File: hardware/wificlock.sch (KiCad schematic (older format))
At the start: 41 parts, among them J1 USB_C_Receptacle_USB2.0, Q1 AO3402, Q2 AO3402, Q3 AO3402, Q4 AO3402, SW1 SW_SPST, SW2 SW_SPST, SW3 SW_SPST, U1 CH340G, U2 ESP-12F, U3 ME6211C33M5G, Y1 12MHz

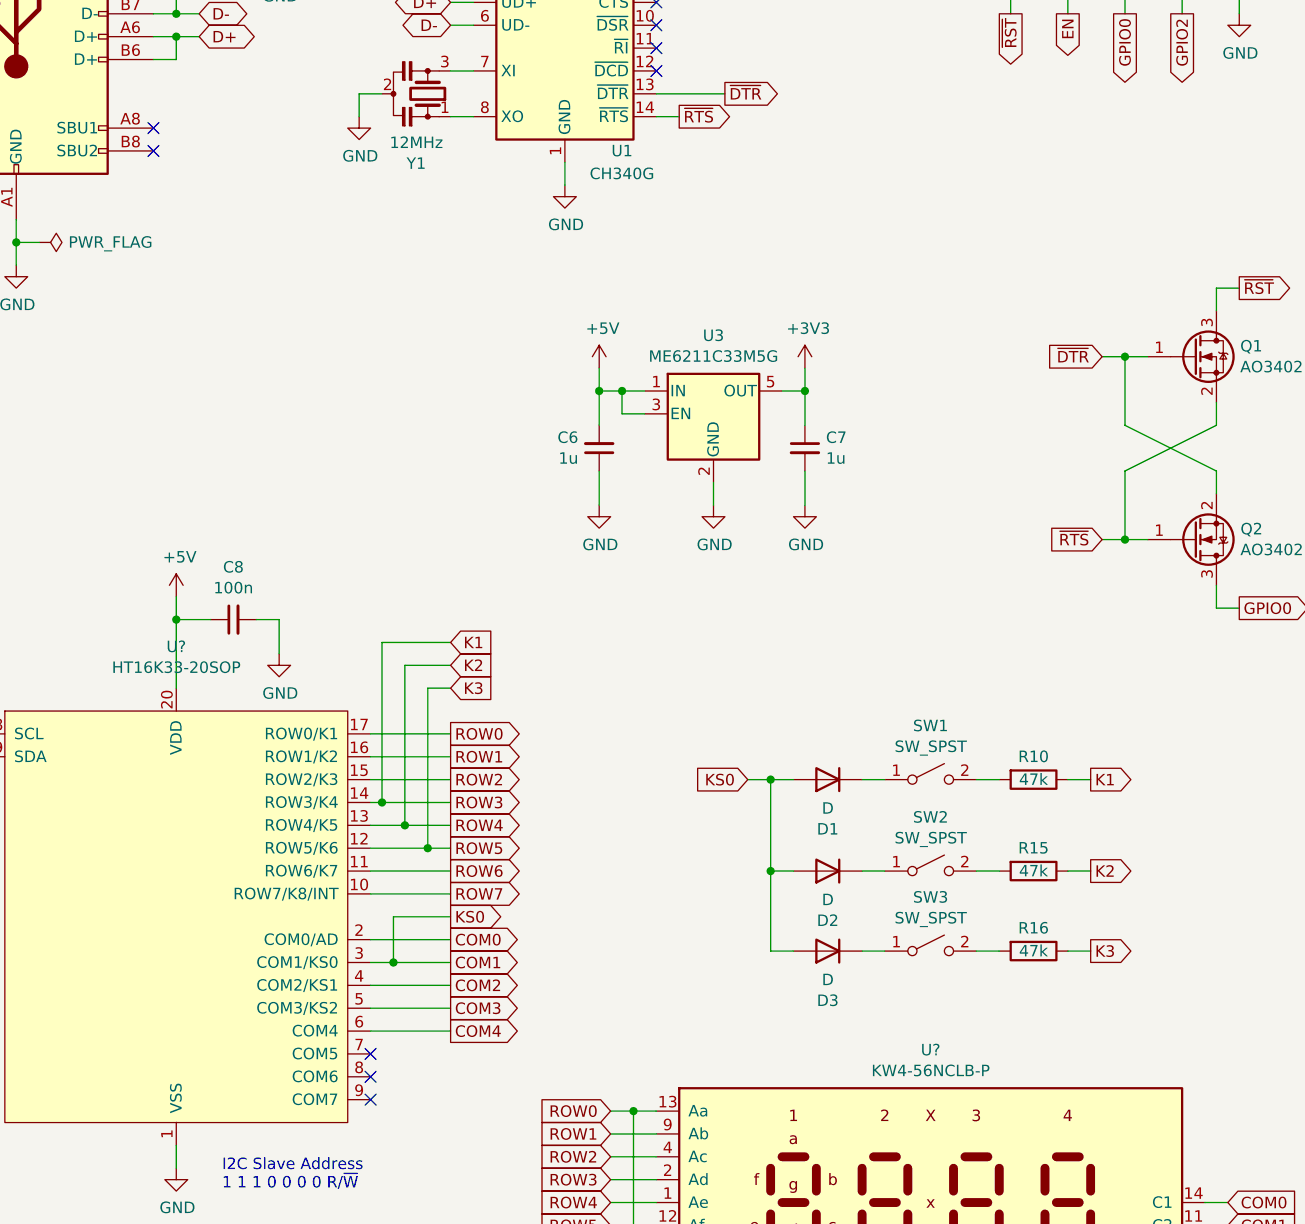
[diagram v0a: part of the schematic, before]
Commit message: add footprints for display and tactile side switch
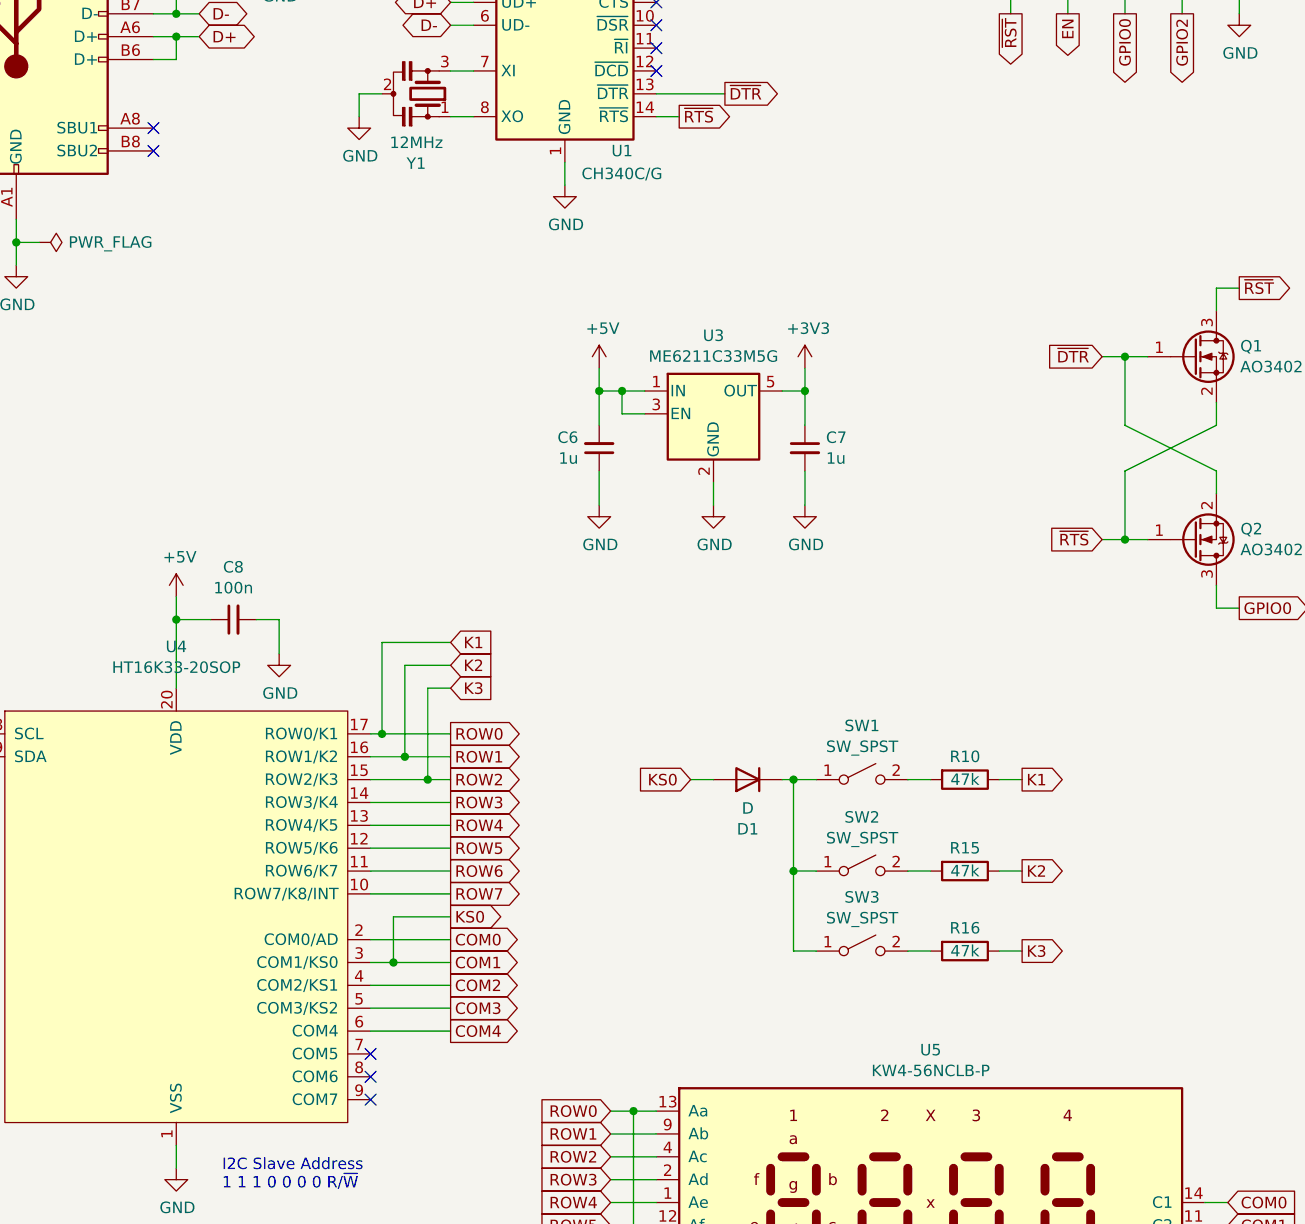
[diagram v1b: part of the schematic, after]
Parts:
- removed D2, D3: D, symbol Device:D
- D1: footprint (none) -> Diode_SMD:D_SOD-123
- R11, R12, R13, R14: footprint (none) -> Resistor_SMD:R_0805_2012Metric
- SW1, SW2, SW3: footprint (none) -> wificlock:Switch-Tactile-3x6x3.5
- U1: value CH340G -> CH340C/G
- U5: renamed from U?; footprint (none) -> wificlock:KW4-56NXLB-P
- Y1: footprint (none) -> Crystal:Resonator_SMD_muRata_CSTxExxV-3Pin_3.0x1.1mm
- gave numbers to parts that had none: 1
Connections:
- net ROW0 is gone; now on net K1: U4.17 (ROW0/K1), U5.13 (Aa), U5.8 (Ax)
- net ROW1 is gone; now on net K2: U4.16 (ROW1/K2), U5.9 (Ab)
- net ROW2 is gone; now on net K3: U4.15 (ROW2/K3), U5.4 (Ac)
- net K1: no longer U4.14 (ROW3/K4), U5.2 (Ad)
- net K2: no longer U4.13 (ROW4/K5), U5.1 (Ae)
- net K3: no longer U4.12 (ROW5/K6), U5.12 (Af)
- net at D1.1 (K), SW1.1 (A): now also SW2.1 (A), SW3.1 (A)
- new net ROW3: U4.14 (ROW3/K4), U5.2 (Ad)
- new net ROW4: U4.13 (ROW4/K5), U5.1 (Ae)
- new net ROW5: U4.12 (ROW5/K6), U5.12 (Af)
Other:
- moved on the sheet: D1, R10, R15, R16, SW1, SW2, SW3
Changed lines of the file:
@@
 P 3550 1700
 F 0 "U1" H 3800 1150 50  0000 C CNN
-F 1 "CH340G" H 3800 1050 50  0000 C CNN
+F 1 "CH340C/G" H 3800 1050 50  0000 C CNN
 F 2 "Package_SO:SOIC-16_3.9x9.9mm_P1.27mm" H 3600 1150 50  0001 L CNN
 F 3 "https://www.mpja.com/download/35227cpdata.pdf" H 3200 2500 50  0001 C CNN
@@
 F 0 "Y1" V 2645 1950 50  0000 C CNN
 F 1 "12MHz" V 2736 1950 50  0000 C CNN
-F 2 "" H 2925 2000 50  0001 C CNN
+F 2 "Crystal:Resonator_SMD_muRata_CSTxExxV-3Pin_3.0x1.1mm" H 2925 2000 50  0001 C CNN
 F 3 "~" H 2925 2000 50  0001 C CNN
 	1    2950 2000
@@
 Wire Wire Line
 	2800 5800 3050 5800
-Text GLabel 4350 5000 0    50   Input ~ 0
-KS0
-$Comp
-L Device:D D1
-U 1 1 60484D0D
-P 4700 5000
-F 0 "D1" H 4700 5217 50  0000 C CNN
-F 1 "D" H 4700 5126 50  0000 C CNN
-F 2 "" H 4700 5000 50  0001 C CNN
-F 3 "~" H 4700 5000 50  0001 C CNN
-	1    4700 5000
-	-1   0    0    1
-$EndComp
-$Comp
-L Switch:SW_SPST SW1
-U 1 1 60486161
-P 5150 5000
-F 0 "SW1" H 5150 5235 50  0000 C CNN
-F 1 "SW_SPST" H 5150 5144 50  0000 C CNN
-F 2 "" H 5150 5000 50  0001 C CNN
-F 3 "~" H 5150 5000 50  0001 C CNN
-	1    5150 5000
-	1    0    0    -1
-$EndComp
-Wire Wire Line
-	4950 5000 4850 5000
-Wire Wire Line
-	4450 5000 4350 5000
-Wire Wire Line
-	4550 5000 4450 5000
-$Comp
-L Device:D D2
-U 1 1 60566D9D
-P 4700 5400
-F 0 "D2" H 4700 5617 50  0000 C CNN
-F 1 "D" H 4700 5526 50  0000 C CNN
-F 2 "" H 4700 5400 50  0001 C CNN
-F 3 "~" H 4700 5400 50  0001 C CNN
-	1    4700 5400
-	-1   0    0    1
-$EndComp
-$Comp
-L Switch:SW_SPST SW2
-U 1 1 605672B7
-P 5150 5400
-F 0 "SW2" H 5150 5635 50  0000 C CNN
-F 1 "SW_SPST" H 5150 5544 50  0000 C CNN
-F 2 "" H 5150 5400 50  0001 C CNN
-F 3 "~" H 5150 5400 50  0001 C CNN
-	1    5150 5400
-	1    0    0    -1
-$EndComp
-Text GLabel 5850 5400 2    50   Output ~ 0
-K2
-Wire Wire Line
-	5850 5400 5750 5400
-Wire Wire Line
-	4950 5400 4850 5400
-Wire Wire Line
-	4450 5000 4450 5400
-Wire Wire Line
-	4450 5400 4550 5400
-Connection ~ 4450 5000
-$Comp
-L Device:D D3
-U 1 1 60586F2B
-P 4700 5750
-F 0 "D3" H 4700 5967 50  0000 C CNN
-F 1 "D" H 4700 5876 50  0000 C CNN
-F 2 "" H 4700 5750 50  0001 C CNN
-F 3 "~" H 4700 5750 50  0001 C CNN
-	1    4700 5750
-	-1   0    0    1
-$EndComp
-Wire Wire Line
-	4450 5400 4450 5750
-Wire Wire Line
-	4450 5750 4550 5750
-Connection ~ 4450 5400
-$Comp
-L Switch:SW_SPST SW3
-U 1 1 60592409
-P 5150 5750
-F 0 "SW3" H 5150 5985 50  0000 C CNN
-F 1 "SW_SPST" H 5150 5894 50  0000 C CNN
-F 2 "" H 5150 5750 50  0001 C CNN
-F 3 "~" H 5150 5750 50  0001 C CNN
-	1    5150 5750
-	1    0    0    -1
-$EndComp
-Text GLabel 5850 5750 2    50   Output ~ 0
-K3
-Wire Wire Line
-	5850 5750 5750 5750
-Wire Wire Line
-	4950 5750 4850 5750
 $Comp
 L power:GND #PWR027
@@
 Wire Wire Line
 	2300 4300 2300 4450
-$Comp
-L Device:R R10
-U 1 1 6067C984
-P 5600 5000
-F 0 "R10" V 5500 5000 50  0000 C CNN
-F 1 "47k" V 5600 5000 50  0000 C CNN
-F 2 "Resistor_SMD:R_0805_2012Metric" V 5530 5000 50  0001 C CNN
-F 3 "~" H 5600 5000 50  0001 C CNN
-	1    5600 5000
-	0    1    1    0
-$EndComp
 Text GLabel 3050 5100 2    50   Output ~ 0
 ROW3
-Wire Wire Line
-	2700 5000 3050 5000
 Text GLabel 3050 5000 2    50   Output ~ 0
 ROW2
-Wire Wire Line
-	2700 4900 3050 4900
 Text GLabel 3050 4900 2    50   Output ~ 0
 ROW1
-Wire Wire Line
-	2700 4800 3050 4800
 Text GLabel 3050 4800 2    50   Output ~ 0
 ROW0
@@
 Wire Wire Line
 	3050 4400 2750 4400
-Wire Wire Line
-	2750 5100 3050 5100
-Wire Wire Line
-	2700 5100 2750 5100
-Connection ~ 2750 5100
-Wire Wire Line
-	2750 4400 2750 5100
-Wire Wire Line
-	2950 5300 2700 5300
-Wire Wire Line
-	2950 4600 2950 5300
 Text GLabel 3050 4600 2    50   Input ~ 0
 K3
 Wire Wire Line
 	3050 4600 2950 4600
-Wire Wire Line
-	2850 5200 2700 5200
-Wire Wire Line
-	2850 4500 2850 5200
 Text GLabel 3050 4500 2    50   Input ~ 0
 K2
 Wire Wire Line
 	3050 4500 2850 4500
-Wire Wire Line
-	5850 5000 5750 5000
-Text GLabel 5850 5000 2    50   Output ~ 0
-K1
 Text Notes 2050 6800 0    50   ~ 0
 I2C Slave Address\n1 1 1 0 0 0 0 R/~W~
-Wire Wire Line
-	5450 5000 5350 5000
-$Comp
-L Device:R R15
-U 1 1 607456CB
-P 5600 5400
-F 0 "R15" V 5500 5400 50  0000 C CNN
-F 1 "47k" V 5600 5400 50  0000 C CNN
-F 2 "Resistor_SMD:R_0805_2012Metric" V 5530 5400 50  0001 C CNN
-F 3 "~" H 5600 5400 50  0001 C CNN
-	1    5600 5400
-	0    1    1    0
-$EndComp
-Wire Wire Line
-	5450 5400 5350 5400
-$Comp
-L Device:R R16
-U 1 1 60745A32
-P 5600 5750
-F 0 "R16" V 5500 5750 50  0000 C CNN
-F 1 "47k" V 5600 5750 50  0000 C CNN
-F 2 "Resistor_SMD:R_0805_2012Metric" V 5530 5750 50  0001 C CNN
-F 3 "~" H 5600 5750 50  0001 C CNN
-	1    5600 5750
-	0    1    1    0
-$EndComp
-Wire Wire Line
-	5450 5750 5350 5750
 $Comp
 L Device:R R14
@@
 F 0 "R14" H 9870 5146 50  0000 L CNN
 F 1 "4k7" H 9870 5055 50  0000 L CNN
-F 2 "" V 9730 5100 50  0001 C CNN
+F 2 "Resistor_SMD:R_0805_2012Metric" V 9730 5100 50  0001 C CNN
 F 3 "~" H 9800 5100 50  0001 C CNN
 	1    9800 5100
@@
 F 0 "R12" H 8670 5146 50  0000 L CNN
 F 1 "4k7" H 8670 5055 50  0000 L CNN
-F 2 "" V 8530 5100 50  0001 C CNN
+F 2 "Resistor_SMD:R_0805_2012Metric" V 8530 5100 50  0001 C CNN
 F 3 "~" H 8600 5100 50  0001 C CNN
 	1    8600 5100
@@
 F 0 "R13" H 9570 5146 50  0000 L CNN
 F 1 "4k7" H 9570 5055 50  0000 L CNN
-F 2 "" V 9430 5100 50  0001 C CNN
+F 2 "Resistor_SMD:R_0805_2012Metric" V 9430 5100 50  0001 C CNN
 F 3 "~" H 9500 5100 50  0001 C CNN
 	1    9500 5100
@@
 F 0 "R11" H 8370 5146 50  0000 L CNN
 F 1 "4k7" H 8370 5055 50  0000 L CNN
-F 2 "" V 8230 5100 50  0001 C CNN
+F 2 "Resistor_SMD:R_0805_2012Metric" V 8230 5100 50  0001 C CNN
 F 3 "~" H 8300 5100 50  0001 C CNN
 	1    8300 5100
@@
 Text GLabel 3050 5200 2    50   Output ~ 0
 ROW4
-Wire Wire Line
-	2850 5200 3050 5200
-Connection ~ 2850 5200
 Text GLabel 3050 5300 2    50   Output ~ 0
 ROW5
-Wire Wire Line
-	2950 5300 3050 5300
-Connection ~ 2950 5300
 Text GLabel 3050 5400 2    50   Output ~ 0
 ROW6
@@
 NoConn ~ 2700 6400
 $Comp
-L wificlock:KW4-56NCLB-P U?
+L wificlock:KW4-56NCLB-P U5
 U 1 1 602B0D2E
 P 5150 6850
-F 0 "U?" H 5150 7517 50  0000 C CNN
+F 0 "U5" H 5150 7517 50  0000 C CNN
 F 1 "KW4-56NCLB-P" H 5150 7426 50  0000 C CNN
-F 2 "" H 5500 6550 50  0001 C CNN
+F 2 "wificlock:KW4-56NXLB-P" H 5500 6550 50  0001 C CNN
 F 3 "https://cdn-shop.adafruit.com/datasheets/865datasheet.pdf" H 5500 6550 50  0001 C CNN
 	1    5150 6850
@@
 $EndComp
 $Comp
-L wificlock:HT16K33-20SOP U?
+L wificlock:HT16K33-20SOP U4
 U 1 1 602D3B7B
 P 1850 5600
-F 0 "U?" H 1850 6781 50  0000 C CNN
+F 0 "U4" H 1850 6781 50  0000 C CNN
 F 1 "HT16K33-20SOP" H 1850 6690 50  0000 C CNN
 F 2 "Package_SO:SOIC-20W_7.5x12.8mm_P1.27mm" H 2550 5650 50  0001 C CNN
@@
 Wire Wire Line
 	3850 6450 3950 6450
+Text GLabel 4100 5000 0    50   Input ~ 0
+KS0
+$Comp
+L Device:D D1
+U 1 1 60484D0D
+P 4350 5000
+F 0 "D1" H 4350 5217 50  0000 C CNN
+F 1 "D" H 4350 5126 50  0000 C CNN
+F 2 "Diode_SMD:D_SOD-123" H 4350 5000 50  0001 C CNN
+F 3 "~" H 4350 5000 50  0001 C CNN
+	1    4350 5000
+	-1   0    0    1
+$EndComp
+$Comp
+L Switch:SW_SPST SW1
+U 1 1 60486161
+P 4850 5000
+F 0 "SW1" H 4850 5235 50  0000 C CNN
+F 1 "SW_SPST" H 4850 5144 50  0000 C CNN
+F 2 "wificlock:Switch-Tactile-3x6x3.5" H 4850 5000 50  0001 C CNN
+F 3 "~" H 4850 5000 50  0001 C CNN
+	1    4850 5000
+	1    0    0    -1
+$EndComp
+Wire Wire Line
+	4550 5000 4500 5000
+$Comp
+L Switch:SW_SPST SW2
+U 1 1 605672B7
+P 4850 5400
+F 0 "SW2" H 4850 5635 50  0000 C CNN
+F 1 "SW_SPST" H 4850 5544 50  0000 C CNN
+F 2 "wificlock:Switch-Tactile-3x6x3.5" H 4850 5400 50  0001 C CNN
+F 3 "~" H 4850 5400 50  0001 C CNN
+	1    4850 5400
+	1    0    0    -1
+$EndComp
+Text GLabel 5550 5400 2    50   Output ~ 0
+K2
+Wire Wire Line
+	5550 5400 5450 5400
+Wire Wire Line
+	4550 5000 4550 5400
+Connection ~ 4550 5000
+Wire Wire Line
+	4550 5400 4550 5750
+Connection ~ 4550 5400
+$Comp
+L Switch:SW_SPST SW3
+U 1 1 60592409
+P 4850 5750
+F 0 "SW3" H 4850 5985 50  0000 C CNN
+F 1 "SW_SPST" H 4850 5894 50  0000 C CNN
+F 2 "wificlock:Switch-Tactile-3x6x3.5" H 4850 5750 50  0001 C CNN
+F 3 "~" H 4850 5750 50  0001 C CNN
+	1    4850 5750
+	1    0    0    -1
+$EndComp
+Text GLabel 5550 5750 2    50   Output ~ 0
+K3
+Wire Wire Line
+	5550 5750 5450 5750
+$Comp
+L Device:R R10
+U 1 1 6067C984
+P 5300 5000
+F 0 "R10" V 5200 5000 50  0000 C CNN
+F 1 "47k" V 5300 5000 50  0000 C CNN
+F 2 "Resistor_SMD:R_0805_2012Metric" V 5230 5000 50  0001 C CNN
+F 3 "~" H 5300 5000 50  0001 C CNN
+	1    5300 5000
+	0    1    1    0
+$EndComp
+Wire Wire Line
+	5550 5000 5450 5000
+Text GLabel 5550 5000 2    50   Output ~ 0
+K1
+Wire Wire Line
+	5150 5000 5050 5000
+$Comp
+L Device:R R15
+U 1 1 607456CB
+P 5300 5400
+F 0 "R15" V 5200 5400 50  0000 C CNN
+F 1 "47k" V 5300 5400 50  0000 C CNN
+F 2 "Resistor_SMD:R_0805_2012Metric" V 5230 5400 50  0001 C CNN
+F 3 "~" H 5300 5400 50  0001 C CNN
+	1    5300 5400
+	0    1    1    0
+$EndComp
+Wire Wire Line
+	5150 5400 5050 5400
+$Comp
+L Device:R R16
+U 1 1 60745A32
+P 5300 5750
+F 0 "R16" V 5200 5750 50  0000 C CNN
+F 1 "47k" V 5300 5750 50  0000 C CNN
+F 2 "Resistor_SMD:R_0805_2012Metric" V 5230 5750 50  0001 C CNN
+F 3 "~" H 5300 5750 50  0001 C CNN
+	1    5300 5750
+	0    1    1    0
+$EndComp
+Wire Wire Line
+	5150 5750 5050 5750
+Wire Wire Line
+	4100 5000 4200 5000
+Wire Wire Line
+	4550 5000 4650 5000
+Wire Wire Line
+	4550 5400 4650 5400
+Wire Wire Line
+	4550 5750 4650 5750
+Wire Wire Line
+	2700 5100 3050 5100
+Wire Wire Line
+	2700 5200 3050 5200
+Wire Wire Line
+	2700 5300 3050 5300
+Wire Wire Line
+	2750 4400 2750 4800
+Wire Wire Line
+	2700 4800 2750 4800
+Wire Wire Line
+	2750 4800 3050 4800
+Connection ~ 2750 4800
+Wire Wire Line
+	2850 4500 2850 4900
+Wire Wire Line
+	2700 4900 2850 4900
+Wire Wire Line
+	2850 4900 3050 4900
+Connection ~ 2850 4900
+Wire Wire Line
+	2950 4600 2950 5000
+Wire Wire Line
+	2700 5000 2950 5000
+Wire Wire Line
+	2950 5000 3050 5000
+Connection ~ 2950 5000
 $EndSCHEMATC

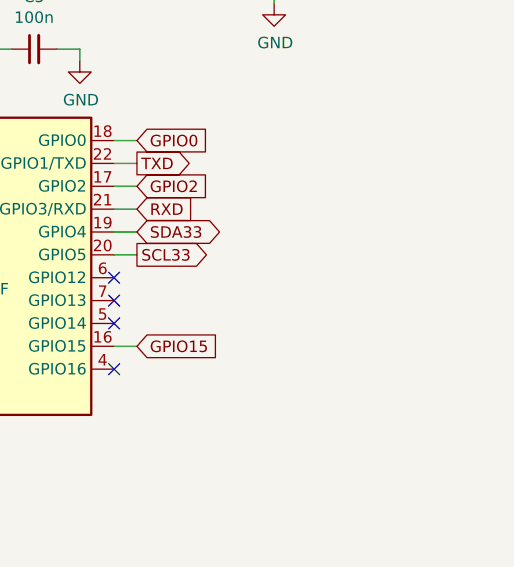
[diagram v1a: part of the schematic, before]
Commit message: add pcb and footprints
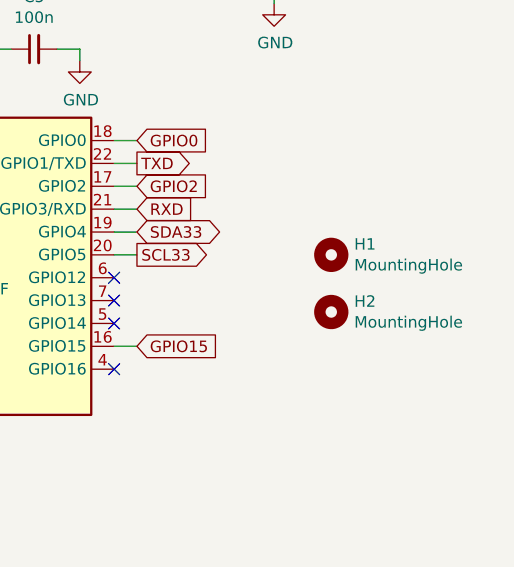
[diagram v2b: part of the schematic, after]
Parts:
- added H1, H2: MountingHole, MountingHole:MountingHole_3.2mm_M3_ISO14580, symbol Mechanical:MountingHole
- J1: footprint Connector_USB:USB_C_Receptacle_XKB_U262-16XN-4BVC11 -> wificlock:USB_C_Receptacle_UT03FD014SX01ZA_Vertical
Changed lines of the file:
@@
 F 0 "J1" H 1257 2517 50  0000 C CNN
 F 1 "USB_C_Receptacle_USB2.0" H 1257 2426 50  0000 C CNN
-F 2 "Connector_USB:USB_C_Receptacle_XKB_U262-16XN-4BVC11" H 1300 1650 50  0001 C CNN
+F 2 "wificlock:USB_C_Receptacle_UT03FD014SX01ZA_Vertical" H 1300 1650 50  0001 C CNN
 F 3 "https://www.usb.org/sites/default/files/documents/usb_type-c.zip" H 1300 1650 50  0001 C CNN
 	1    1150 1650
@@
 	2950 5000 3050 5000
 Connection ~ 2950 5000
+$Comp
+L Mechanical:MountingHole H1
+U 1 1 6062D568
+P 9950 2800
+F 0 "H1" H 10050 2846 50  0000 L CNN
+F 1 "MountingHole" H 10050 2755 50  0000 L CNN
+F 2 "MountingHole:MountingHole_3.2mm_M3_ISO14580" H 9950 2800 50  0001 C CNN
+F 3 "~" H 9950 2800 50  0001 C CNN
+	1    9950 2800
+	1    0    0    -1
+$EndComp
+$Comp
+L Mechanical:MountingHole H2
+U 1 1 6062E0E2
+P 9950 3050
+F 0 "H2" H 10050 3096 50  0000 L CNN
+F 1 "MountingHole" H 10050 3005 50  0000 L CNN
+F 2 "MountingHole:MountingHole_3.2mm_M3_ISO14580" H 9950 3050 50  0001 C CNN
+F 3 "~" H 9950 3050 50  0001 C CNN
+	1    9950 3050
+	1    0    0    -1
+$EndComp
 $EndSCHEMATC
